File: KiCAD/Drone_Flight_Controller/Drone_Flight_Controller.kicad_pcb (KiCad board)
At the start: 2 copper layers, 100 x 100 mm, 92 parts, among them J301 Conn_01x03_Pin, J302 Conn_01x04, J303 Conn_01x03_Pin, J304 XT60, J305 Conn_01x03_Pin, J306 Conn_01x03_Pin, P701 USB_C_Plug_USB2.0, Q201 BUJ303B,127, Q301 BC846C, Q302 BC846C, Q303 BC856C, Q304 BC846C, Q305 BC856C, Q306 BC856C, Q307 BC856C, Q309 BC846C, Q501 2N2222A, Q701 BC846C, Q702 BC846C, Q703 BC846C, Q704 BC846C, Q705 BC846C, Q706 BC846C, Q707 BC846C, U201 MCP1501-33xCH, U202 AS358, U203 AS358, U301 AS358, U302 AS358, U305 AS358, U401 ESP32-WROOM-32, U402 DPS368, U403 BNO055, U701 MCP2200-I-SO, Y701 CSTNE12M0GH5L000R0

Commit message: Preliminary fotprint placement
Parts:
- removed BZ501: Buzzer, Buzzer_Beeper:Buzzer_TDK_PS1240P02BT_D12.2mm_H6.5mm
- removed C305: 22u, Capacitor_THT:CP_Radial_D5.0mm_P2.00mm
- removed C306, C307, C308, C309, C310: 100n, Capacitor_SMD:C_0805_2012Metric_Pad1.18x1.45mm_HandSolder
- removed C401: 120nF, Capacitor_SMD:C_0805_2012Metric_Pad1.18x1.45mm_HandSolder
- removed C402: 1uF, Capacitor_SMD:C_0805_2012Metric_Pad1.18x1.45mm_HandSolder
- removed D702, D703, D704, D705: LED, LED_SMD:LED_0805_2012Metric_Pad1.15x1.40mm_HandSolder
- removed D706: RxLED, LED_SMD:LED_0805_2012Metric_Pad1.15x1.40mm_HandSolder
- removed D707: TxLED, LED_SMD:LED_0805_2012Metric_Pad1.15x1.40mm_HandSolder
- removed H301, H302, H303, H304: MountingHole_Pad, MountingHole:MountingHole_3.2mm_M3_Pad_TopBottom
- removed J301, J303, J305, J306: Conn_01x03_Pin, Connector_PinHeader_2.54mm:PinHeader_1x03_P2.54mm_Vertical
- removed J302: Conn_01x04, Connector_PinHeader_2.54mm:PinHeader_1x04_P2.54mm_Vertical
- removed J304: XT60, Connector_AMASS:AMASS_XT60-F_1x02_P7.20mm_Vertical
- removed NT201: NetTie_2, NetTie:NetTie-2_SMD_Pad2.0mm
- removed P701: USB_C_Plug_USB2.0, Connector_PinHeader_2.54mm:PinHeader_1x07_P2.54mm_Vertical
- removed Q301, Q302, Q304, Q309, Q701, Q702, Q703, Q704, Q705, Q706, Q707: BC846C, Package_TO_SOT_SMD:SOT-23
- removed Q303, Q305, Q306, Q307: BC856C, Package_TO_SOT_SMD:SOT-23
- removed Q501: 2N2222A, Package_TO_SOT_THT:TO-92_HandSolder
- removed R207, R208: 20k, Resistor_SMD:R_0805_2012Metric_Pad1.20x1.40mm_HandSolder
- removed R701: 10k, Resistor_SMD:R_0805_2012Metric_Pad1.20x1.40mm_HandSolder
- removed R702, R703, R704, R705, R706, R707, R708: 110k, Resistor_SMD:R_0805_2012Metric_Pad1.20x1.40mm_HandSolder
- removed U203, U305: AS358, Package_SO:SO-8_3.9x4.9mm_P1.27mm
- removed U401: ESP32-WROOM-32, RF_Module:ESP32-WROOM-32
- removed U402: DPS368, Package_LGA:Bosch_LGA-8_2x2.5mm_P0.65mm_ClockwisePinNumbering
- removed U403: BNO055, Package_LGA:LGA-28_5.2x3.8mm_P0.5mm
- removed Y701: CSTNE12M0GH5L000R0, Crystal:Resonator_SMD_Murata_CSTxExxV-3Pin_3.0x1.1mm
- added BZ401: Buzzer, Buzzer_Beeper:Buzzer_TDK_PS1240P02BT_D12.2mm_H6.5mm, F.Cu at (186.1, 143.0)
- added C203: 100n, Capacitor_SMD:C_0805_2012Metric_Pad1.18x1.45mm_HandSolder, F.Cu at (31.0, 39.9)
- added C204: 100n, Capacitor_SMD:C_0805_2012Metric_Pad1.18x1.45mm_HandSolder, F.Cu at (31.0, 43.0)
- added C205: 22u, Capacitor_THT:CP_Radial_D5.0mm_P2.00mm, F.Cu at (84.5, 96.5)
- added C206: 100n, Capacitor_SMD:C_0805_2012Metric_Pad1.18x1.45mm_HandSolder, F.Cu at (31.0, 46.0)
- added C207: 100n, Capacitor_SMD:C_0805_2012Metric_Pad1.18x1.45mm_HandSolder, F.Cu at (31.0, 49.0)
- added C208: 100n, Capacitor_SMD:C_0805_2012Metric_Pad1.18x1.45mm_HandSolder, F.Cu at (31.0, 52.0)
- added C209: 100n, Capacitor_SMD:C_0805_2012Metric_Pad1.18x1.45mm_HandSolder, F.Cu at (31.0, 55.0)
- added C210: 100n, Capacitor_SMD:C_0805_2012Metric_Pad1.18x1.45mm_HandSolder, F.Cu at (31.0, 58.0)
- added C701: 100µF, Capacitor_THT:CP_Radial_D5.0mm_P2.00mm, F.Cu at (99.4, 145.0)
- added C702: 330µF, Capacitor_THT:CP_Radial_D6.3mm_P2.50mm, F.Cu at (110.9, 142.8)
- added D202: 1N4148, Diode_SMD:D_SOD-323_HandSoldering, F.Cu at (204.8, 85.0)
- added D203: 1N4148, Diode_SMD:D_SOD-323_HandSoldering, F.Cu at (204.8, 83.0)
- added D204: BAT60BE6359HTMA1, Diode_SMD:D_SOD-323_HandSoldering, F.Cu at (200.8, 115.0)
- added D205: 1N4148, Diode_SMD:D_SOD-323_HandSoldering, F.Cu at (204.8, 112.0)
- added D206: 1N4148, Diode_SMD:D_SOD-323_HandSoldering, F.Cu at (204.8, 110.0)
- added D207: BAT60BE6359HTMA1, Diode_SMD:D_SOD-323_HandSoldering, F.Cu at (95.2, 115.5)
- added D208: 1N4148, Diode_SMD:D_SOD-323_HandSoldering, F.Cu at (91.2, 110.0)
- added D209: 1N4148, Diode_SMD:D_SOD-323_HandSoldering, F.Cu at (91.2, 112.0)
- added D210: BAT60BE6359HTMA1, Diode_SMD:D_SOD-323_HandSoldering, F.Cu at (95.2, 79.5)
- added D211: 1N4148, Diode_SMD:D_SOD-323_HandSoldering, F.Cu at (91.2, 83.0)
- added D212: 1N4148, Diode_SMD:D_SOD-323_HandSoldering, F.Cu at (91.2, 85.0)
- added D213: LED, LED_SMD:LED_0805_2012Metric_Pad1.15x1.40mm_HandSolder, F.Cu at (68.5, 161.5)
- added D214: LED, LED_SMD:LED_0805_2012Metric_Pad1.15x1.40mm_HandSolder, F.Cu at (72.0, 161.5)
- added D215: LED, LED_SMD:LED_0805_2012Metric_Pad1.15x1.40mm_HandSolder, F.Cu at (75.5, 161.5)
- added D601: BAT60BE6359HTMA1, Diode_SMD:D_SOD-323_HandSoldering, F.Cu at (24.8, 107.0)
- added D602: LED, LED_SMD:LED_0805_2012Metric_Pad1.15x1.40mm_HandSolder, F.Cu at (265.5, 155.5)
- added D603: LED, LED_SMD:LED_0805_2012Metric_Pad1.15x1.40mm_HandSolder, F.Cu at (261.5, 155.5)
- added D604: LED, LED_SMD:LED_0805_2012Metric_Pad1.15x1.40mm_HandSolder, F.Cu at (257.5, 155.5)
- added D605: LED, LED_SMD:LED_0805_2012Metric_Pad1.15x1.40mm_HandSolder, F.Cu at (253.5, 155.5)
- added D606: LED, LED_SMD:LED_0805_2012Metric_Pad1.15x1.40mm_HandSolder, F.Cu at (249.5, 155.5)
- added D607: RxLED, LED_SMD:LED_0805_2012Metric_Pad1.15x1.40mm_HandSolder, F.Cu at (245.4, 155.5)
- added D608: TxLED, LED_SMD:LED_0805_2012Metric_Pad1.15x1.40mm_HandSolder, F.Cu at (241.5, 155.6)
- added H201: MountingHole_Pad, MountingHole:MountingHole_3.2mm_M3_Pad_TopBottom, F.Cu at (221.0, 80.0)
- added H202: MountingHole_Pad, MountingHole:MountingHole_3.2mm_M3_Pad_TopBottom, F.Cu at (221.0, 115.0)
- added H203: MountingHole_Pad, MountingHole:MountingHole_3.2mm_M3_Pad_TopBottom, F.Cu at (75.0, 80.0)
- added H204: MountingHole_Pad, MountingHole:MountingHole_3.2mm_M3_Pad_TopBottom, F.Cu at (75.0, 115.0)
- added J201: Conn_01x04, Connector_PinHeader_2.54mm:PinHeader_1x04_P2.54mm_Vertical, F.Cu at (179.0, 37.5)
- added J205: XT60, Connector_AMASS:AMASS_XT60-F_1x02_P7.20mm_Vertical, F.Cu at (77.0, 101.1)
- added L701: 100µH, Inductor_SMD:L_1210_3225Metric_Pad1.42x2.65mm_HandSolder, F.Cu at (100.4, 149.5)
- added Motor1: Conn_01x03_Pin, Connector_PinHeader_2.54mm:PinHeader_1x03_P2.54mm_Vertical, F.Cu at (209.9, 80.0)
- added Motor2: Conn_01x03_Pin, Connector_PinHeader_2.54mm:PinHeader_1x03_P2.54mm_Vertical, F.Cu at (210.5, 115.0)
- added Motor3: Conn_01x03_Pin, Connector_PinHeader_2.54mm:PinHeader_1x03_P2.54mm_Vertical, F.Cu at (86.1, 115.0)
- added Motor4: Conn_01x03_Pin, Connector_PinHeader_2.54mm:PinHeader_1x03_P2.54mm_Vertical, F.Cu at (86.1, 80.0)
- added Q202: BC856C, Package_TO_SOT_SMD:SOT-23, F.Cu at (210.0, 83.9)
- added Q203: BC846C, Package_TO_SOT_SMD:SOT-23, F.Cu at (215.0, 111.1)
- added Q204: BC856C, Package_TO_SOT_SMD:SOT-23, F.Cu at (210.0, 111.0)
- added Q205: BC846C, Package_TO_SOT_SMD:SOT-23, F.Cu at (81.0, 110.9)
- added Q206: BC856C, Package_TO_SOT_SMD:SOT-23, F.Cu at (86.0, 111.1)
- added Q207: BC846C, Package_TO_SOT_SMD:SOT-23, F.Cu at (81.0, 84.1)
- added Q208: BC856C, Package_TO_SOT_SMD:SOT-23, F.Cu at (86.0, 83.9)
- added Q401: 2N2222A, Package_TO_SOT_THT:TO-92_HandSolder, F.Cu at (192.6, 152.5)
- added Q601: BC846C, Package_TO_SOT_SMD:SOT-23, F.Cu at (264.4, 150.5)
- added Q602: BC846C, Package_TO_SOT_SMD:SOT-23, F.Cu at (260.6, 150.5)
- added Q603: BC846C, Package_TO_SOT_SMD:SOT-23, F.Cu at (256.6, 150.5)
- added Q604: BC846C, Package_TO_SOT_SMD:SOT-23, F.Cu at (252.6, 150.5)
- added Q605: BC846C, Package_TO_SOT_SMD:SOT-23, F.Cu at (248.4, 150.5)
- added Q606: BC846C, Package_TO_SOT_SMD:SOT-23, F.Cu at (244.4, 150.5)
- added Q607: BC846C, Package_TO_SOT_SMD:SOT-23, F.Cu at (240.4, 150.5)
- added R303: 10k, Resistor_SMD:R_0805_2012Metric_Pad1.20x1.40mm_HandSolder, F.Cu at (148.0, 132.0)
- added R503: 2.7k, Resistor_SMD:R_0805_2012Metric_Pad1.20x1.40mm_HandSolder, F.Cu at (38.5, 150.5)
- added R504: 20k, Resistor_SMD:R_0805_2012Metric_Pad1.20x1.40mm_HandSolder, F.Cu at (39.0, 160.0)
- added R505: 82k, Resistor_SMD:R_0805_2012Metric_Pad1.20x1.40mm_HandSolder, F.Cu at (35.0, 160.0)
- added R506: 2.7k, Resistor_SMD:R_0805_2012Metric_Pad1.20x1.40mm_HandSolder, F.Cu at (35.0, 163.5)
- added R607: 110k, Resistor_SMD:R_0805_2012Metric_Pad1.20x1.40mm_HandSolder, F.Cu at (245.5, 142.5)
- added R608: 110k, Resistor_SMD:R_0805_2012Metric_Pad1.20x1.40mm_HandSolder, F.Cu at (243.5, 142.5)
- added U205: AS358, Package_SO:SO-8_3.9x4.9mm_P1.27mm, F.Cu at (40.4, 155.9)
- added U303: ESP32-WROOM-32, RF_Module:ESP32-WROOM-32, F.Cu at (218.5, 97.6)
- added U601: MCP2200-I-SO, Package_SO:SOIC-20W_7.5x12.8mm_P1.27mm, F.Cu at (244.1, 133.9)
- added Y601: CSTNE12M0GH5L000R0, Crystal:Resonator_SMD_Murata_CSTxExxV-3Pin_3.0x1.1mm, F.Cu at (240.3, 141.5)
- C201, C202: value 22u -> 100n; footprint Capacitor_THT:CP_Radial_D5.0mm_P2.00mm -> Capacitor_SMD:C_0805_2012Metric_Pad1.18x1.45mm_HandSolder
- C301: value 100n -> 1µF
- C302: value 100n -> 120nF
- C304: value 100n -> 1uF
- D201: value 1N4148 -> BAT60BE6359HTMA1; footprint Diode_THT:D_DO-35_SOD27_P7.62mm_Horizontal -> Diode_SMD:D_SOD-323_HandSoldering
- D701: value LED -> 1N5822; footprint LED_SMD:LED_0805_2012Metric_Pad1.15x1.40mm_HandSolder -> Diode_THT:D_DO-201AD_P15.24mm_Horizontal
- Q201: value BUJ303B,127 -> BC846C; footprint Package_TO_SOT_THT:TO-220-3_Horizontal_TabDown -> Package_TO_SOT_SMD:SOT-23
- R201: value 2.7k -> 10k
- R202: value 300k -> 20k
- R203: value 1.1k -> 20k
- R204: value 1.1k -> 10k
- R205: value 16 -> 10k; footprint Resistor_THT:R_Axial_Power_L48.0mm_W12.5mm_P60.96mm -> Resistor_SMD:R_0805_2012Metric_Pad1.20x1.40mm_HandSolder; moved to F.Cu
- R206: value 2k -> 10k
- R301, R601: value 20k -> 10k
- R302: value 20k -> 2.7k
- R401: value 10k -> 1k
- R501: value 1k -> 20k
- R502: value 180 -> 82k
- R602, R605: value 82k -> 110k
- R603, R606: value 2.7k -> 110k
- R604: value 20k -> 110k
- U201: value MCP1501-33xCH -> AS358; footprint Package_TO_SOT_SMD:SOT-23-6 -> Package_SO:SO-8_3.9x4.9mm_P1.27mm
- U301: value AS358 -> DPS368; footprint Package_SO:SO-8_3.9x4.9mm_P1.27mm -> Package_LGA:Bosch_LGA-8_2x2.5mm_P0.65mm_ClockwisePinNumbering
- U302: value AS358 -> BNO055; footprint Package_SO:SO-8_3.9x4.9mm_P1.27mm -> Package_LGA:LGA-28_5.2x3.8mm_P0.5mm
- U701: value MCP2200-I-SO -> LM2576-3.3WT; footprint Package_SO:SOIC-20W_7.5x12.8mm_P1.27mm -> Package_TO_SOT_THT:TO-220-5_Vertical
- moved R501 194.7 mm to (35.0, 156.5), turned to -90 degrees
- moved C202 188.1 mm to (31.0, 36.9), turned to 0 degrees
- moved R502 186.6 mm to (42.5, 150.5), turned to 180 degrees
- moved C201 172.3 mm to (31.0, 33.9), turned to 0 degrees
- moved R602 118.5 mm to (263.5, 142.5)
- moved R603 113.6 mm to (261.5, 142.5), turned to -90 degrees
- moved G*** 103.2 mm to (257.0, 59.0)
- moved R206 103.0 mm to (91.0, 79.5), turned to 180 degrees
- moved R604 98.0 mm to (251.5, 142.5)
- moved R605 93.1 mm to (249.5, 142.5)
- moved R601 90.7 mm to (240.5, 144.5), turned to 0 degrees
- moved C301 90.1 mm to (155.0, 132.0), turned to 180 degrees
- moved R606 88.3 mm to (247.5, 142.5), turned to -90 degrees
- moved U701 86.7 mm to (105.9, 147.4), turned to 90 degrees
- moved U302 78.2 mm to (136.4, 39.2), turned to 0 degrees
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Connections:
- C201 pad 1: Net-(U201-~{SHDN}) -> +3V3
- C201 pad 2: -BATT -> GND
- C202 pad 1: +3.3V -> +3V3
- C301 pad 1: +3.3V -> GND
- C301 pad 2: GND -> Net-(U303-EN)
- C302 pad 1: +3.3V -> +3V3
- C303 pad 1: +3.3V -> GND
- C303 pad 2: GND -> Net-(U303-EN)
- C304 pad 1: +3.3V -> Net-(U302-CAP)
- D201 pad 1: Net-(D201-K) -> +4V76
- D201 pad 2: +3.3V -> Net-(D201-A)
- D701 pad 2: +5V -> GND
- Q201 pad 1: Net-(Q201-C) -> Net-(D202-A)
- Q201 pad 2: Net-(D201-K) -> Net-(Motor1-Pin_1)
- Q201 pad 3: +3.3V -> Net-(D201-A)
- R201 pad 1: +BATT -> Net-(R201-Pad1)
- R201 pad 2: Net-(U201-VDD) -> Net-(D202-K)
- R202 pad 1: Net-(U203A-+) -> +3V3
- R202 pad 2: Net-(U203B-+) -> +1V7
- R203 pad 1: Net-(U201-VDD) -> +1V7
- R203 pad 2: Net-(U201-~{SHDN}) -> GND
- R204 pad 1: Net-(U201-VDD) -> Net-(R204-Pad1)
- R204 pad 2: -BATT -> Net-(D205-K)
- R205 pad 1: +BATT -> Net-(R205-Pad1)
- R205 pad 2: Net-(Q201-C) -> Net-(D208-K)
- R206 pad 2: Net-(U203A-+) -> Net-(D211-K)
- R301 pad 1: +3.3V -> Net-(U302-~{BOOT_LOAD_PIN})
- R301 pad 2: +1V7 -> +3V3
- R302 pad 1: +1V7 -> Net-(U303-IO0)
- R302 pad 2: GND -> ~{Programming}
- R401 pad 1: Net-(U401-IO4) -> +3V3
- R401 pad 2: +3.3V -> Net-(BZ401--)
- R501 pad 1: +3.3V -> Net-(U205A-+)
- R501 pad 2: Net-(BZ501--) -> -BATT
- R502 pad 1: Buzzer -> +BATT
- R601 pad 1: Net-(U302A-+) -> +3V3
- R601 pad 2: -BATT -> Net-(U601-RST)
- R602 pad 1: +BATT -> Net-(U601-GP0/SSPND)
- R602 pad 2: Net-(R602-Pad2) -> Net-(Q601-B)
- R603 pad 1: Net-(R602-Pad2) -> Net-(U601-GP1/USB-CFG)
- R603 pad 2: Net-(U302A-+) -> Net-(Q602-B)
- R604 pad 1: +3.3V -> Net-(Q603-B)
- R604 pad 2: Net-(U302A--) -> Net-(U601-GP3)
- R605 pad 1: Net-(U302A--) -> Net-(U601-GP4)
- R605 pad 2: Net-(R605-Pad2) -> Net-(Q604-B)
- R606 pad 1: Net-(R605-Pad2) -> Net-(U601-GP5)
- R606 pad 2: Net-(U302B-+) -> Net-(Q605-B)
- U201 pad 1: Net-(U201-OUT) -> Net-(R201-Pad1)
- U201 pad 2: -BATT -> Motor2
- U201 pad 3: -BATT -> Motor1
- U201 pad 4: Net-(U201-~{SHDN}) -> -BATT
- U201 pad 5: -BATT -> Motor2
- U201 pad 6: Net-(U201-VDD) -> +1V7
- U202 pad 1: Net-(U202A--) -> Net-(R205-Pad1)
- U202 pad 2: Net-(U202A--) -> +1V7
- U202 pad 3: Net-(U201-OUT) -> Motor3
- U202 pad 5: Net-(U202A--) -> Motor4
- U202 pad 6: Net-(U202B--) -> +1V7
- U301 pad 1: Net-(Q303-B) -> GND
- U301 pad 2: +1V7 -> Net-(U301-~{CS})
- U301 pad 3: Motor1 -> Net-(U301-SDI)
- U301 pad 4: -BATT -> Net-(U301-SCK)
- U301 pad 5: Motor2 -> Net-(U301-SDO)
- U301 pad 6: +1V7 -> +3V3
- U301 pad 7: Net-(Q301-B) -> GND
- U301 pad 8: +BATT -> +3V3
- U302 pad 1: Net-(U302B-+) -> unconnected-(U302-PIN1-Pad1)
- U302 pad 2: Net-(U302A--) -> GND
- U302 pad 3: Net-(U302A-+) -> +3V3
- U302 pad 4: -BATT -> Net-(U302-~{BOOT_LOAD_PIN})
- U302 pad 5: Net-(U302B-+) -> +3V3
- U302 pad 6: BATT Monitor -> GND
- U302 pad 7: BATT Monitor -> unconnected-(U302-PIN7-Pad7)
- U302 pad 8: +BATT -> unconnected-(U302-PIN8-Pad8)
- U701 pad 1: +3.3V -> 4V76
- U701 pad 2: Net-(U701-OSC1) -> Net-(D701-K)
- U701 pad 3: Net-(U701-OSC2) -> GND
- U701 pad 4: Net-(U701-RST) -> +3V3
- U701 pad 5: Net-(U701-GP7/TxLED) -> GND
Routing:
- net GND: track 306.5 -> 0.00 mm, vias 48 -> 0
- net +BATT: track 288.3 -> 0.00 mm, vias 3 -> 0
- net -BATT: track 255.5 -> 0.00 mm, vias 3 -> 0
- net BATT Monitor: track 99.5 -> 0.00 mm, vias 2 -> 0
- net +3.3V: track 90.0 -> 0.00 mm, vias 5 -> 0
- net Net-(P701-D+): track 76.9 -> 0.00 mm, vias 1 -> 0
- net Net-(P701-D-): track 73.5 -> 0.00 mm, vias 1 -> 0
- net Net-(Q303-B): track 64.5 -> 0.00 mm
- net Motor3: track 63.8 -> 0.00 mm
- net Programming TX: track 62.5 -> 0.00 mm, vias 2 -> 0
- net Programming RTS: track 62.4 -> 0.00 mm, vias 2 -> 0
- net Net-(Q302-B): track 61.8 -> 0.00 mm
- net Programming RX: track 59.1 -> 0.00 mm, vias 2 -> 0
- net Net-(Q304-B): track 57.3 -> 0.00 mm, vias 2 -> 0
- net Programming CTS: track 54.1 -> 0.00 mm, vias 2 -> 0
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- removed copper zone on B.Cu, net +3.3V
- removed copper zone on F.Cu, net GND
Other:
- board size 100 x 100 mm -> 156 x 45 mm
- board text removed: "+5V"
- board text removed: "+5V NC NC D- D+ GND SHIELD"
- board text removed: "3V3"
- board text removed: "GND"
- board text removed: "PWM"
- board text removed: "PfUSCH"
- board text removed: "RX"
- board text removed: "TX"

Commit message: Change to 2-sided assembly
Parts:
- added P601: USB_C_Plug_USB2.0, Connector_USB:USB_C_Receptacle_HRO_TYPE-C-31-M-12, F.Cu at (245.0, 140.0)
- C301, C303, D201, D202, D203, D204, D205, D206, D207, D208, D209, D210, D211, D212, Q201, Q202, Q203, Q204, Q205, Q206, Q207, Q208, Q601, Q602, Q603, Q604, Q605, Q606, Q607, R201, R202, R203, R204, R205, R206, R302, R303, R401, R501, R502, R503, R504, R505, R506, R601, R602, R603, R604, R605, R606, R607, R608, U201, U202, U205: moved to B.Cu
- U701: footprint Package_TO_SOT_THT:TO-220-5_Vertical -> Package_TO_SOT_THT:TO-220-5_Horizontal_TabDown
- moved R303 88.3 mm to (224.0, 87.0), turned to 180 degrees
- moved C303 83.2 mm to (221.0, 86.0)
- moved C301 76.6 mm to (217.0, 87.0), turned to 0 degrees
- moved D602 13.8 mm to (252.8, 161.0)
- moved D603 13.8 mm to (248.8, 161.0)
- moved D604 13.8 mm to (244.8, 161.0)
- moved D605 13.8 mm to (240.8, 161.0)
- moved D606 13.8 mm to (236.8, 161.0)
- moved D607 13.8 mm to (232.7, 161.0)
- moved Q601 13.8 mm to (251.7, 156.0), turned to 180 degrees
- moved Q602 13.8 mm to (247.9, 156.1), turned to 180 degrees
- moved Q603 13.8 mm to (243.9, 156.1), turned to 180 degrees
- moved Q604 13.8 mm to (239.9, 156.0), turned to 180 degrees
- moved Q605 13.8 mm to (235.7, 156.0), turned to 180 degrees
- moved Q606 13.8 mm to (231.7, 156.1), turned to 180 degrees
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
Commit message: part placement and routing
part placement and routing
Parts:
- removed D213: LED, LED_SMD:LED_0805_2012Metric_Pad1.15x1.40mm_HandSolder
- added J207: Conn_01x05, Connector_PinHeader_2.54mm:PinHeader_1x05_P2.54mm_Vertical, F.Cu at (104.4, 115.1)
- added R208: 75, Resistor_SMD:R_0805_2012Metric_Pad1.20x1.40mm_HandSolder, F.Cu at (89.7, 84.7)
- added R209: 150, Resistor_SMD:R_0805_2012Metric_Pad1.20x1.40mm_HandSolder, F.Cu at (93.7, 84.7)
- added R402: 180, Resistor_SMD:R_0805_2012Metric_Pad1.20x1.40mm_HandSolder, B.Cu at (123.8, 102.0)
- C208, C209, C210, C302, C304, D601, R301, U302: moved to B.Cu
- C301, Q601, Q602, Q603, Q604, Q605, Q606, Q607: moved to F.Cu
- moved D602 174.9 mm to (97.8, 80.0), turned to 90 degrees
- moved Q601 170.6 mm to (96.8, 84.8)
- moved D603 167.8 mm to (101.9, 80.0), turned to 90 degrees
- moved R602 165.6 mm to (97.8, 84.7)
- moved Q602 163.4 mm to (100.8, 84.8)
- moved R603 160.0 mm to (101.9, 84.7)
- moved D604 153.8 mm to (114.0, 80.0), turned to 90 degrees
- moved D607 150.4 mm to (105.9, 80.0), turned to 90 degrees
- moved Q603 149.0 mm to (113.0, 84.8)
- moved D605 147.0 mm to (118.1, 80.0), turned to 90 degrees
- moved Q606 145.5 mm to (104.9, 84.8)
- moved D608 143.8 mm to (110.0, 80.0), turned to 90 degrees
- moved Q604 141.9 mm to (117.1, 84.8)
- moved R607 141.8 mm to (105.9, 84.7)
- moved D606 140.4 mm to (122.2, 80.0), turned to 90 degrees
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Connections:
- Q603 pad 2: -BATT -> GND
- Q604 pad 2: -BATT -> GND
- Q605 pad 2: -BATT -> GND
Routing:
- net +3V3: track 0.00 -> 194.4 mm, vias 0 -> 6
- net GND: track 0.00 -> 176.2 mm, vias 0 -> 9
- net +BATT: track 0.00 -> 131.5 mm, vias 0 -> 4
- net +4V76: track 0.00 -> 129.2 mm, vias 0 -> 2
- net -BATT: track 0.00 -> 99.1 mm, vias 0 -> 3
- net BATT Monitor: track 0.00 -> 85.3 mm, vias 0 -> 3
- net +1V7: track 0.00 -> 64.1 mm
- net Programming TX: track 0.00 -> 60.5 mm, vias 0 -> 2
- net Motor3: track 0.00 -> 59.0 mm, vias 0 -> 1
- net Programming RTS: track 0.00 -> 57.0 mm, vias 0 -> 2
- net Programming RX: track 0.00 -> 55.4 mm, vias 0 -> 2
- net IO1: track 0.00 -> 50.8 mm, vias 0 -> 2
- net Net-(U302-~{RESET}): track 0.00 -> 48.8 mm, vias 0 -> 1
- net Programming CTS: track 0.00 -> 47.7 mm, vias 0 -> 2
- net IO2: track 0.00 -> 46.3 mm, vias 0 -> 2
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- added copper zone on B.Cu, net +3V3
- added copper zone on F.Cu, net GND
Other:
- board size 156 x 45 mm -> 83 x 45.1 mm

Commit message: extend board length
extend board length
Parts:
- moved C209 3.05 mm to (83.8, 100.8)
- moved U202 2.79 mm to (87.6, 105.1)
- moved U701 2.78 mm to (99.0, 109.4)
- moved C701 2.68 mm to (104.0, 109.5)
- moved C702 2.68 mm to (104.0, 103.0)
- moved C205 2.68 mm to (81.8, 96.5)
- moved C210 2.68 mm to (83.7, 90.4)
- moved D701 2.68 mm to (102.5, 97.5)
- moved J205 2.68 mm to (74.3, 101.1)
- moved R202 2.68 mm to (93.8, 102.7)
- moved R501 2.68 mm to (99.7, 92.7)
- moved R502 2.68 mm to (93.1, 88.8)
- moved R503 2.68 mm to (93.1, 92.7)
- moved R504 2.68 mm to (96.4, 92.7)
- moved R505 2.68 mm to (96.4, 88.8)
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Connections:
- C205 pad 2: -BATT -> GND
- C206 pad 2: -BATT -> GND
- C207 pad 2: -BATT -> GND
- C208 pad 2: -BATT -> GND
- C209 pad 2: -BATT -> GND
- C210 pad 2: -BATT -> GND
- C701 pad 1: 4V76 -> +4V76
- J205 pad 1: -BATT -> GND
- R501 pad 2: -BATT -> GND
- U201 pad 4: -BATT -> GND
- U202 pad 4: -BATT -> GND
- U205 pad 4: -BATT -> GND
- U701 pad 1: 4V76 -> +4V76
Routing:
- net -BATT: track 99.1 -> 0.00 mm, vias 3 -> 0
- net GND: track 176.2 -> 265.5 mm, vias 9 -> 12
- net Motor4: track 0.00 -> 55.6 mm, vias 0 -> 3
- net +1V7: track 64.1 -> 44.2 mm, vias 0 -> 2
- net Net-(D701-K): track 19.8 -> 11.7 mm
- net 4V76: track 5.05 -> 0.00 mm
- net +4V76: track 129.2 -> 133.6 mm
- net Motor3: track 59.0 -> 62.1 mm
- net Net-(U601-RST): track 14.5 -> 17.2 mm
- net Net-(D207-A): track 18.9 -> 16.5 mm
- net Net-(R206-Pad1): track 38.1 -> 35.8 mm
- net Buzzer: track 27.9 -> 30.2 mm
- net Net-(Q601-B): track 1.83 -> 3.78 mm
- net Net-(U601-GP1/USB-CFG): track 21.8 -> 23.3 mm
- net BATT Monitor: track 85.3 -> 86.5 mm
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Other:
- board size 83 x 45.1 mm -> 85 x 45 mm

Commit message: Fixing errors
Fixing errors
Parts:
- added SW1: SW_Push, Button_Switch_SMD:SW_Push_1P1T_NO_CK_KSC6xxJ, F.Cu at (129.1, 107.5)
- moved G*** 135.6 mm to (148.0, 139.7), turned to -90 degrees
- moved C201 103.0 mm to (123.2, 91.7)
- moved G*** 23.7 mm to (127.5, 135.4)
- moved Q401 16.7 mm to (110.0, 111.1), turned to 90 degrees
- moved R401 3.78 mm to (120.3, 103.3)
- moved BZ401 2.03 mm to (116.2, 106.9)
- moved R402 1.81 mm to (122.7, 103.4), turned to -90 degrees
- moved R301 1.63 mm to (118.0, 97.7)
- moved U302 1.37 mm to (110.8, 97.5)
- moved C302 1.37 mm to (115.0, 97.6)
- moved Y601 0.97 mm to (123.8, 88.6), turned to -90 degrees
- moved C203 0.85 mm to (36.1, 42.9)
- moved C304 0.72 mm to (112.5, 101.3)
- moved H202 0.34 mm to (148.0, 115.0)
- moved H201 0.34 mm to (148.0, 80.0)
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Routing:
- net GND: track 265.5 -> 333.2 mm, vias 12 -> 14
- net Net-(U303-EN): track 14.6 -> 50.4 mm, vias 1 -> 3
- net +1V7: track 44.2 -> 67.0 mm
- net Net-(Q401-B): track 5.34 -> 16.8 mm, vias 0 -> 1
- net Net-(BZ401--): track 6.90 -> 16.1 mm
- net +3V3: track 195.5 -> 204.5 mm
- net Net-(D701-K): track 11.7 -> 19.2 mm
- net Net-(U303-IO0): track 24.1 -> 31.3 mm
- net Net-(R204-Pad1): track 21.1 -> 28.1 mm
- net Net-(U301-SCK): track 29.8 -> 25.6 mm, vias 0 -> 2
- net IO3: track 39.4 -> 42.8 mm
- net Net-(R206-Pad1): track 35.8 -> 38.4 mm
- net Buzzer: track 30.2 -> 27.7 mm
- net Net-(U601-OSC2): track 6.37 -> 8.54 mm
- net Net-(U302-~{RESET}): track 48.8 -> 50.7 mm
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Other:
- outline, holes or cut-outs redrawn

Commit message: Fix Schematic PCB parity
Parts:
- removed SW1: SW_Push, Button_Switch_SMD:SW_Push_1P1T_NO_CK_KSC6xxJ
- added SW301: SW_Push, Button_Switch_SMD:SW_Push_1P1T_NO_CK_KSC6xxJ, F.Cu at (129.1, 107.5)
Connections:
- P601 pad A6: Net-(P601-D+) -> Net-(U601-D+)
- P601 pad A7: Net-(P601-D-) -> Net-(U601-D-)
- P601 pad B6: (no net) -> Net-(U601-D+)
- P601 pad B7: (no net) -> Net-(U601-D-)
- U601 pad 18: Net-(P601-D-) -> Net-(U601-D-)
- U601 pad 19: Net-(P601-D+) -> Net-(U601-D+)
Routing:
- net Net-(U601-D-): track 0.00 -> 20.3 mm
- net Net-(P601-D-): track 20.3 -> 0.00 mm
- net Net-(U601-D+): track 0.00 -> 20.0 mm
- net Net-(P601-D+): track 20.0 -> 0.00 mm

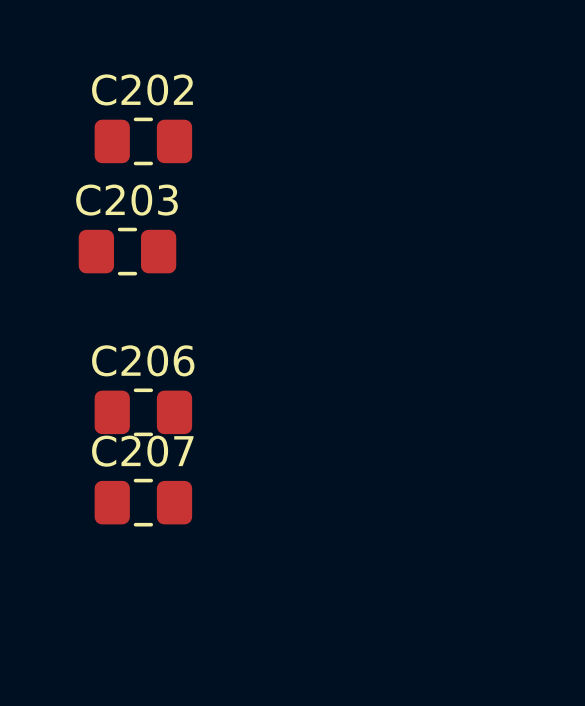
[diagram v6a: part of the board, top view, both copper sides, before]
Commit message: Remove unneeded Capacitors
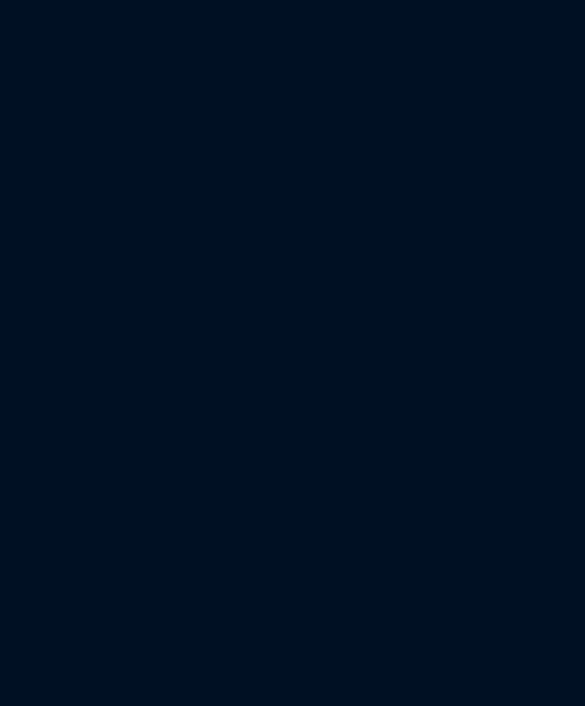
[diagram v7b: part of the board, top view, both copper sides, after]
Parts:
- removed C202, C203, C206, C207: 100n, Capacitor_SMD:C_0805_2012Metric_Pad1.18x1.45mm_HandSolder

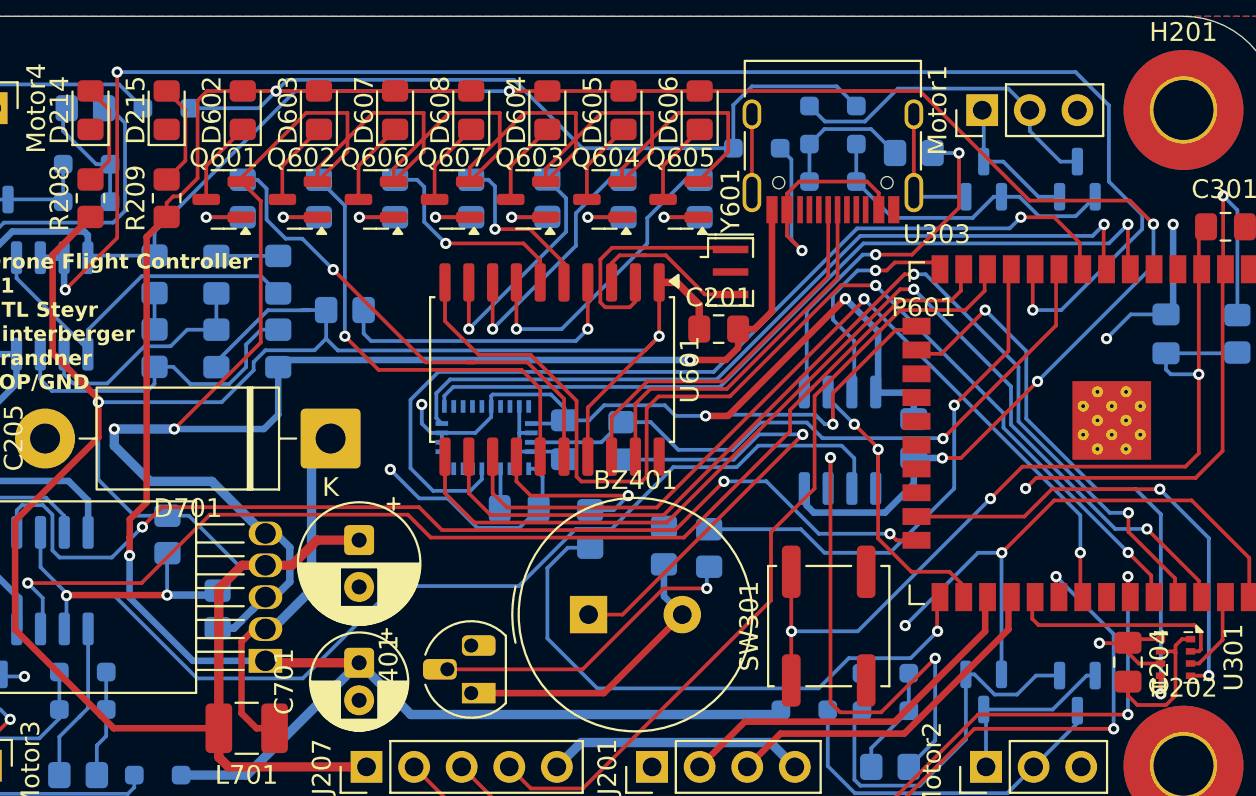
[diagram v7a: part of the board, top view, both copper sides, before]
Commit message: Fix DRC Errors
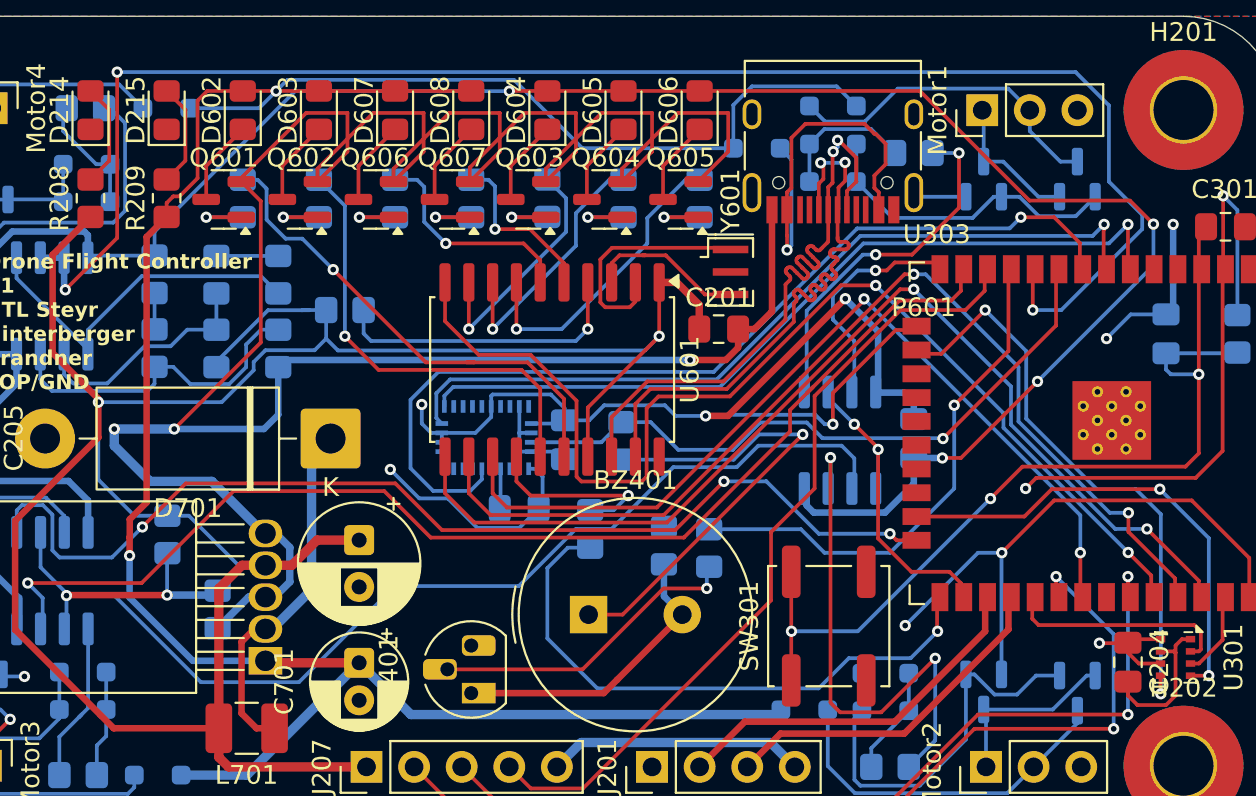
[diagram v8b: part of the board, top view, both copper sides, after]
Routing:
- net Net-(U601-D-): track 20.3 -> 33.2 mm, vias 0 -> 2
- net Net-(U601-D+): track 20.0 -> 31.5 mm, vias 0 -> 2
- net GND: track 333.2 -> 325.2 mm
- net Net-(D601-A): track 15.6 -> 21.5 mm
- net Motor4: track 55.6 -> 56.6 mm
- net Motor3: track 62.1 -> 63.2 mm
